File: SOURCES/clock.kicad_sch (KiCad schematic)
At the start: 15 parts, among them P22 TST, P28 TST, P29 TST, P30 TST, U10 IDT2309NZ, X1 ASV-24.576MHz-EJ-T

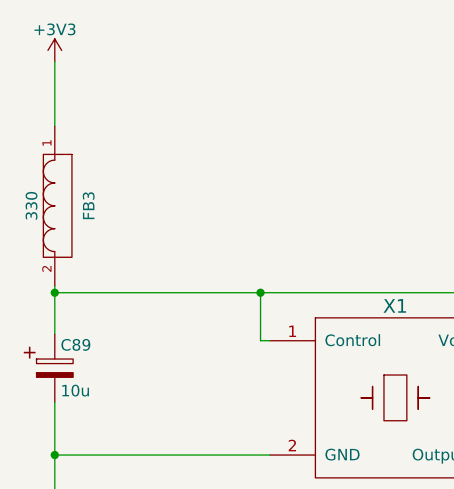
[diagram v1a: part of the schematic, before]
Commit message: Removed redundant 7414 and pot, rerouted a bit.
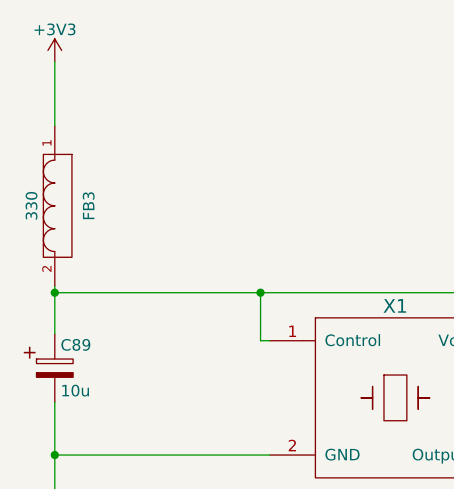
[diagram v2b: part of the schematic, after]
